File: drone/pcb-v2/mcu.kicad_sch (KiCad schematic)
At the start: 26 parts, among them J1 Conn_01x02_Pin, SW2 SW_Push, U2 STM32F103C8Tx, U3 TLV1117LV33DCYR, U4 W25Q128JVS, Y1 Crystal

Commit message: [pcb] schematic v2: footprint/part assignments
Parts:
- C10: renamed from C5; footprint (none) -> Capacitor_SMD:C_0603_1608Metric; LCSC (none) -> C14663
- C11: renamed from C13; footprint Capacitor_SMD:C_0805_2012Metric_Pad1.18x1.45mm_HandSolder -> Capacitor_SMD:C_0603_1608Metric; LCSC (none) -> C14663
- C12: renamed from C14; footprint Capacitor_SMD:C_0805_2012Metric_Pad1.18x1.45mm_HandSolder -> Capacitor_SMD:C_0603_1608Metric; LCSC (none) -> C14663
- C13: renamed from C31; footprint Capacitor_SMD:C_0805_2012Metric_Pad1.18x1.45mm_HandSolder -> Capacitor_SMD:C_0603_1608Metric; LCSC (none) -> C14663
- C14: renamed from C15; now left out of the parts list
- C15: renamed from C6; now left out of the parts list
- C16: renamed from C7; now left out of the parts list
- C17: renamed from C8; now left out of the parts list
- C18: renamed from C9; footprint Capacitor_SMD:C_0805_2012Metric_Pad1.18x1.45mm_HandSolder -> Capacitor_SMD:C_0603_1608Metric; LCSC (none) -> C14663
- C19, C20: renamed from C10; footprint Capacitor_SMD:C_0603_1608Metric_Pad1.08x0.95mm_HandSolder -> Capacitor_SMD:C_0603_1608Metric; LCSC (none) -> C1648
- C9: renamed from C4; footprint (none) -> Capacitor_SMD:C_0603_1608Metric; LCSC (none) -> C15849
- J3: renamed from J1; now left out of the parts list
- R15: renamed from R1; footprint Resistor_SMD:R_0805_2012Metric_Pad1.20x1.40mm_HandSolder -> Resistor_SMD:R_0603_1608Metric; LCSC (none) -> C25803
- R16: renamed from R2; footprint Resistor_SMD:R_0805_2012Metric_Pad1.20x1.40mm_HandSolder -> Resistor_SMD:R_0603_1608Metric; LCSC (none) -> C25803
- R17: renamed from R3; footprint Resistor_SMD:R_0805_2012Metric_Pad1.20x1.40mm_HandSolder -> Resistor_SMD:R_0805_2012Metric; LCSC (none) -> C17414
- SW3: renamed from SW2; now left out of the parts list
- TP4: now left out of the parts list
- U4: renamed from U3; now left out of the parts list
- U5: renamed from U2; LCSC (none) -> C8734
- U6: renamed from U4; LCSC (none) -> C97521
- renumbered JP1 to JP2

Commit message: [pcb] pcb v2: component placement
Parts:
- removed JP2: SolderJumper_3_Open, Jumper:SolderJumper-3_P1.3mm_Open_RoundedPad1.0x1.5mm, symbol Jumper:SolderJumper_3_Open
- added SW4: SW_SPDT, Button_Switch_THT:SW_Slide-03_Wuerth-WS-SLTV_10x2.5x6.4_P2.54mm, symbol Switch:SW_SPDT
- C14: footprint Capacitor_SMD:C_0805_2012Metric_Pad1.18x1.45mm_HandSolder -> Capacitor_SMD:C_0603_1608Metric; LCSC (none) -> C19702; now in the parts list
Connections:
- net +3.3V: now also SW4.3 (C)
- net GND: now also SW4.1 (A)
- net at R17.1: now also SW4.2 (B)
- net ISC1_SCL renamed I2C1_SCL
- net ISC1_SDA renamed I2C1_SDA
- no-connect marks 0 -> 1
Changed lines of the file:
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@@
 	)
 	(rectangle
-		(start 104.14 20.32)
+		(start 99.06 20.32)
 		(end 168.91 43.18)
 		(stroke
@@
 		(color 0 0 0 0)
 	)
+	(no_connect
+		(at 127 74.93)
+	)
 	(wire
 		(pts
@@
 		)
 	)
-	(global_label "ISC1_SCL"
+	(global_label "I2C1_SCL"
 		(shape input)
 		(at 31.75 82.55 180)
@@
 		)
 	)
-	(global_label "ISC1_SDA"
+	(global_label "I2C1_SDA"
 		(shape input)
 		(at 31.75 85.09 180)
@@
 	(symbol
 		(lib_id "power:GND")
-		(at 128.27 82.55 270)
+		(at 121.92 80.01 270)
 		(unit 1)
 		(exclude_from_sim no)
@@
 		(fields_autoplaced yes)
 		(property "Reference" "#PWR056"
-			(at 121.92 82.55 0)
+			(at 115.57 80.01 0)
 			(effects
 				(font
@@
 		)
 		(property "Value" "GND"
-			(at 124.46 82.5499 90)
+			(at 118.11 80.0099 90)
 			(effects
 				(font
@@
 		)
 		(property "Footprint" ""
-			(at 128.27 82.55 0)
+			(at 121.92 80.01 0)
 			(effects
 				(font
@@
 		)
 		(property "Datasheet" ""
-			(at 128.27 82.55 0)
+			(at 121.92 80.01 0)
 			(effects
 				(font
@@
 		)
 		(property "Description" "Power symbol creates a global label with name \"GND\" , ground"
-			(at 128.27 82.55 0)
+			(at 121.92 80.01 0)
 			(effects
 				(font
@@
 	)
 	(symbol
-		(lib_id "Jumper:SolderJumper_3_Open")
-		(at 128.27 77.47 90)
-		(unit 1)
-		(exclude_from_sim no)
-		(in_bom no)
-		(on_board yes)
-		(dnp no)
-		(fields_autoplaced yes)
-		(property "Reference" "JP2"
-			(at 125.73 76.1999 90)
-			(effects
-				(font
-					(size 1.27 1.27)
-				)
-				(justify left)
-			)
-		)
-		(property "Value" "SolderJumper_3_Open"
-			(at 125.73 78.7399 90)
-			(effects
-				(font
-					(size 1.27 1.27)
-				)
-				(justify left)
-			)
-		)
-		(property "Footprint" "Jumper:SolderJumper-3_P1.3mm_Open_RoundedPad1.0x1.5mm"
-			(at 128.27 77.47 0)
-			(effects
-				(font
-					(size 1.27 1.27)
-				)
-				(hide yes)
-			)
-		)
-		(property "Datasheet" "~"
-			(at 128.27 77.47 0)
-			(effects
-				(font
-					(size 1.27 1.27)
-				)
-				(hide yes)
-			)
-		)
-		(property "Description" "Solder Jumper, 3-pole, open"
-			(at 128.27 77.47 0)
-			(effects
-				(font
-					(size 1.27 1.27)
-				)
-				(hide yes)
-			)
-		)
-		(pin "1"
-		)
-		(pin "2"
-		)
-		(pin "3"
-		)
-		(instances
-			(project "astra-v2"
-				(path "/e7184c3b-9f46-4a4e-9d8d-c6d386a497ae/418bc491-5de4-4ac8-8f4b-e13307d6b42a"
-					(reference "JP2")
-					(unit 1)
-				)
-			)
-		)
-	)
-	(symbol
 		(lib_id "Device:C")
 		(at 113.03 30.48 0)
@@
 	)
 	(symbol
+		(lib_id "Switch:SW_SPDT")
+		(at 127 77.47 180)
+		(unit 1)
+		(exclude_from_sim no)
+		(in_bom yes)
+		(on_board yes)
+		(dnp no)
+		(fields_autoplaced yes)
+		(property "Reference" "SW4"
+			(at 127 68.58 0)
+			(effects
+				(font
+					(size 1.27 1.27)
+				)
+			)
+		)
+		(property "Value" "SW_SPDT"
+			(at 127 71.12 0)
+			(effects
+				(font
+					(size 1.27 1.27)
+				)
+			)
+		)
+		(property "Footprint" "Button_Switch_THT:SW_Slide-03_Wuerth-WS-SLTV_10x2.5x6.4_P2.54mm"
+			(at 127 77.47 0)
+			(effects
+				(font
+					(size 1.27 1.27)
+				)
+				(hide yes)
+			)
+		)
+		(property "Datasheet" "~"
+			(at 127 69.85 0)
+			(effects
+				(font
+					(size 1.27 1.27)
+				)
+				(hide yes)
+			)
+		)
+		(property "Description" "Switch, single pole double throw"
+			(at 127 77.47 0)
+			(effects
+				(font
+					(size 1.27 1.27)
+				)
+				(hide yes)
+			)
+		)
+		(pin "3"
+		)
+		(pin "1"
+		)
+		(pin "2"
+		)
+		(instances
+			(project ""
+				(path "/e7184c3b-9f46-4a4e-9d8d-c6d386a497ae/418bc491-5de4-4ac8-8f4b-e13307d6b42a"
+					(reference "SW4")
+					(unit 1)
+				)
+			)
+		)
+	)
+	(symbol
 		(lib_id "power:+BATT")
 		(at 213.36 59.69 270)
@@
 		(unit 1)
 		(exclude_from_sim no)
-		(in_bom no)
+		(in_bom yes)
 		(on_board yes)
 		(dnp no)
@@
 			)
 		)
-		(property "Footprint" "Capacitor_SMD:C_0805_2012Metric_Pad1.18x1.45mm_HandSolder"
+		(property "Footprint" "Capacitor_SMD:C_0603_1608Metric"
 			(at 141.9352 34.29 0)
 			(effects
@@
 			)
 		)
+		(property "LCSC" "C19702"
+			(at 140.97 30.48 90)
+			(effects
+				(font
+					(size 1.27 1.27)
+				)
+				(hide yes)
+			)
+		)
 		(pin "1"
 		)
@@
 	(symbol
 		(lib_id "power:+3.3V")
-		(at 128.27 72.39 90)
+		(at 121.92 74.93 90)
 		(unit 1)
 		(exclude_from_sim no)
@@
 		(fields_autoplaced yes)
 		(property "Reference" "#PWR053"
-			(at 132.08 72.39 0)
+			(at 125.73 74.93 0)
 			(effects
 				(font
@@
 		)
 		(property "Value" "+3.3V"
-			(at 124.46 72.3899 90)
+			(at 118.11 74.9299 90)
 			(effects
 				(font
@@
 		)
 		(property "Footprint" ""
-			(at 128.27 72.39 0)
+			(at 121.92 74.93 0)
 			(effects
 				(font
@@
 		)
 		(property "Datasheet" ""
-			(at 128.27 72.39 0)
+			(at 121.92 74.93 0)
 			(effects
 				(font
@@
 		)
 		(property "Description" "Power symbol creates a global label with name \"+3.3V\""
-			(at 128.27 72.39 0)
+			(at 121.92 74.93 0)
 			(effects
 				(font

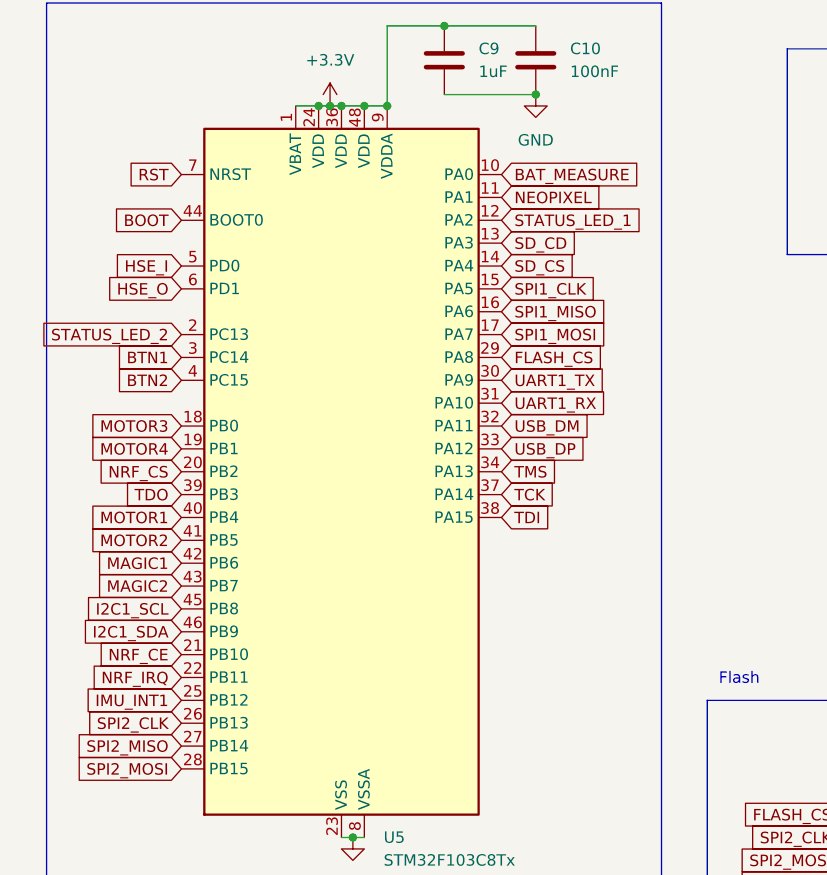
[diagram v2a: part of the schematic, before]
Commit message: [pcb] finish routing
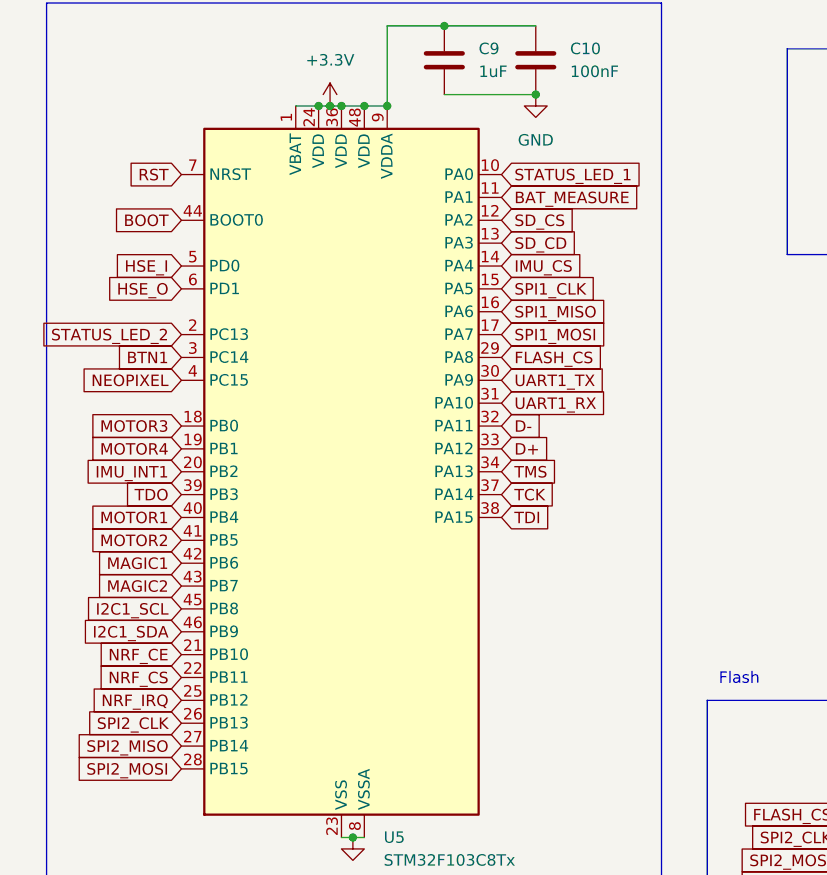
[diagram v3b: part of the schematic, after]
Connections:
- net BTN2 is gone; now on net NEOPIXEL: U5.4 (PC15)
- net BAT_MEASURE: now also U5.11 (PA1); no longer U5.10 (PA0)
- net IMU_INT1: now also U5.20 (PB2); no longer U5.25 (PB12)
- net NEOPIXEL: no longer U5.11 (PA1)
- net NRF_CS: now also U5.22 (PB11); no longer U5.20 (PB2)
- net NRF_IRQ: now also U5.25 (PB12); no longer U5.22 (PB11)
- net SD_CS: now also U5.12 (PA2); no longer U5.14 (PA4)
- net STATUS_LED_1: now also U5.10 (PA0); no longer U5.12 (PA2)
- net USB_DM renamed D-
- net USB_DP renamed D+
- new net IMU_CS: U5.14 (PA4)

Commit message: [pcb] drc fixes
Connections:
- net IMU_CS: now also U5.13 (PA3); no longer U5.14 (PA4)
- net SD_CD: now also U5.14 (PA4); no longer U5.13 (PA3)
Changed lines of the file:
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@@
+		)
+	)
+	(global_label "IMU_CS"
+		(shape input)
+		(at 67.31 41.91 0)
+		(fields_autoplaced yes)
+		(effects
+			(font
+				(size 1.27 1.27)
+			)
+			(justify left)
+		)
+		(property "Intersheetrefs" "${INTERSHEET_REFS}"
+			(at 77.129 41.91 0)
+			(effects
+				(font
+					(size 1.27 1.27)
+				)
+				(justify left)
+				(hide yes)
+			)
 		)
 	)
@@
 		)
 	)
+	(global_label "SD_CD"
+		(shape input)
+		(at 67.31 44.45 0)
+		(fields_autoplaced yes)
+		(effects
+			(font
+				(size 1.27 1.27)
+			)
+			(justify left)
+		)
+		(property "Intersheetrefs" "${INTERSHEET_REFS}"
+			(at 76.2823 44.45 0)
+			(effects
+				(font
+					(size 1.27 1.27)
+				)
+				(justify left)
+				(hide yes)
+			)
+		)
+	)
 	(global_label "RST"
 		(shape input)
@@
 		)
 	)
-	(global_label "IMU_CS"
-		(shape input)
-		(at 67.31 44.45 0)
-		(fields_autoplaced yes)
-		(effects
-			(font
-				(size 1.27 1.27)
-			)
-			(justify left)
-		)
-		(property "Intersheetrefs" "${INTERSHEET_REFS}"
-			(at 77.129 44.45 0)
-			(effects
-				(font
-					(size 1.27 1.27)
-				)
-				(justify left)
-				(hide yes)
-			)
-		)
-	)
 	(global_label "SPI2_MOSI"
 		(shape input)
@@
 			(effects
 				(font
-					(size 1.27 1.27)
-				)
-				(justify left)
-				(hide yes)
-			)
-		)
-	)
-	(global_label "SD_CD"
-		(shape input)
-		(at 67.31 41.91 0)
-		(fields_autoplaced yes)
-		(effects
-			(font
-				(size 1.27 1.27)
-			)
-			(justify left)
-		)
-		(property "Intersheetrefs" "${INTERSHEET_REFS}"
-			(at 76.2823 41.91 0)
-			(effects
-				(font
